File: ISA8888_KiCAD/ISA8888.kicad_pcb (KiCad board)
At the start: 2 copper layers, 154.8 x 106.2 mm, 65 parts, among them J1 Bus_PCI_32bit_Universal, J2 Bus_ISA_16bit, J3 AEN/BALE/TC J3, J4 Crystal J4, J5 PCI Jumpers, J6 PPDGNT# Motherboard Redirect, J7 PPDREQ# Motherboard Redirect, U2 SMROM-AT24CS02, U3 -5v MAX660, Y1 CFPS-72

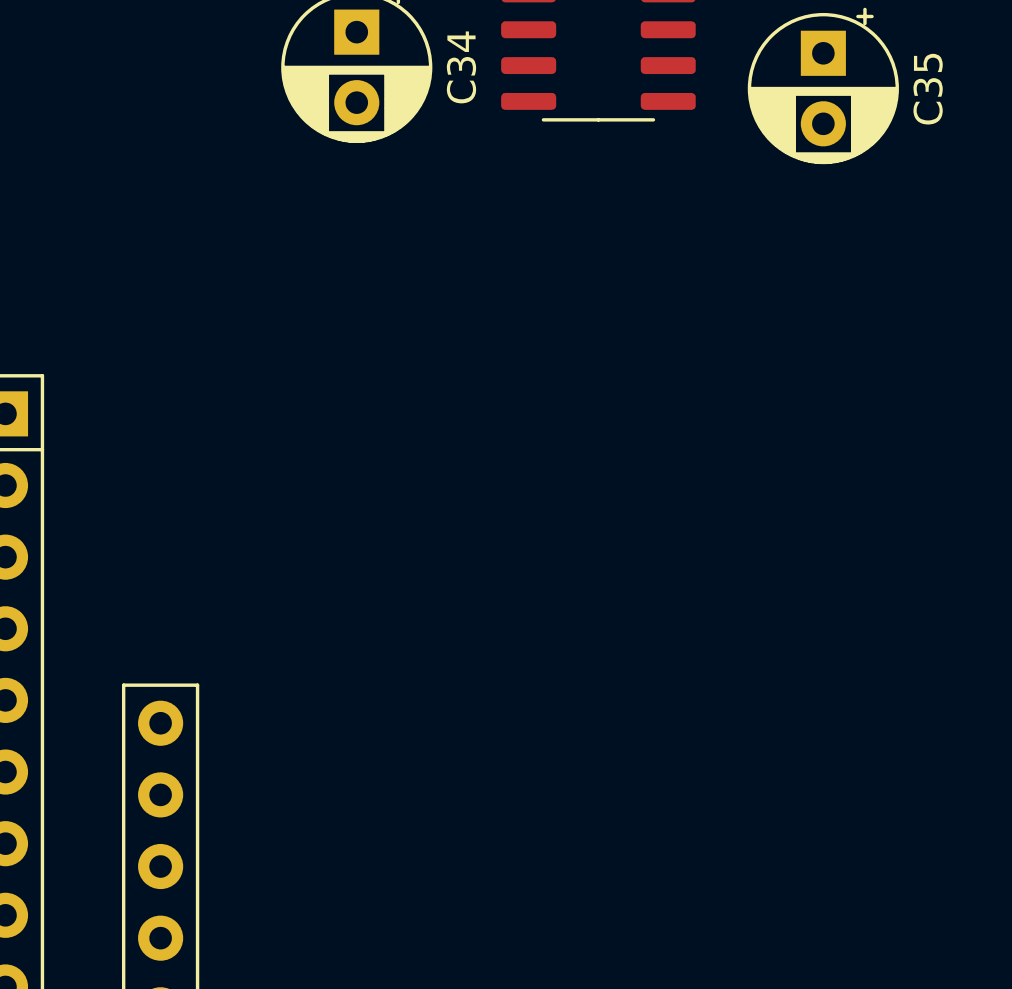
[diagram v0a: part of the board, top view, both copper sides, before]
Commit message: New SCH sheet "Power and Configuration"
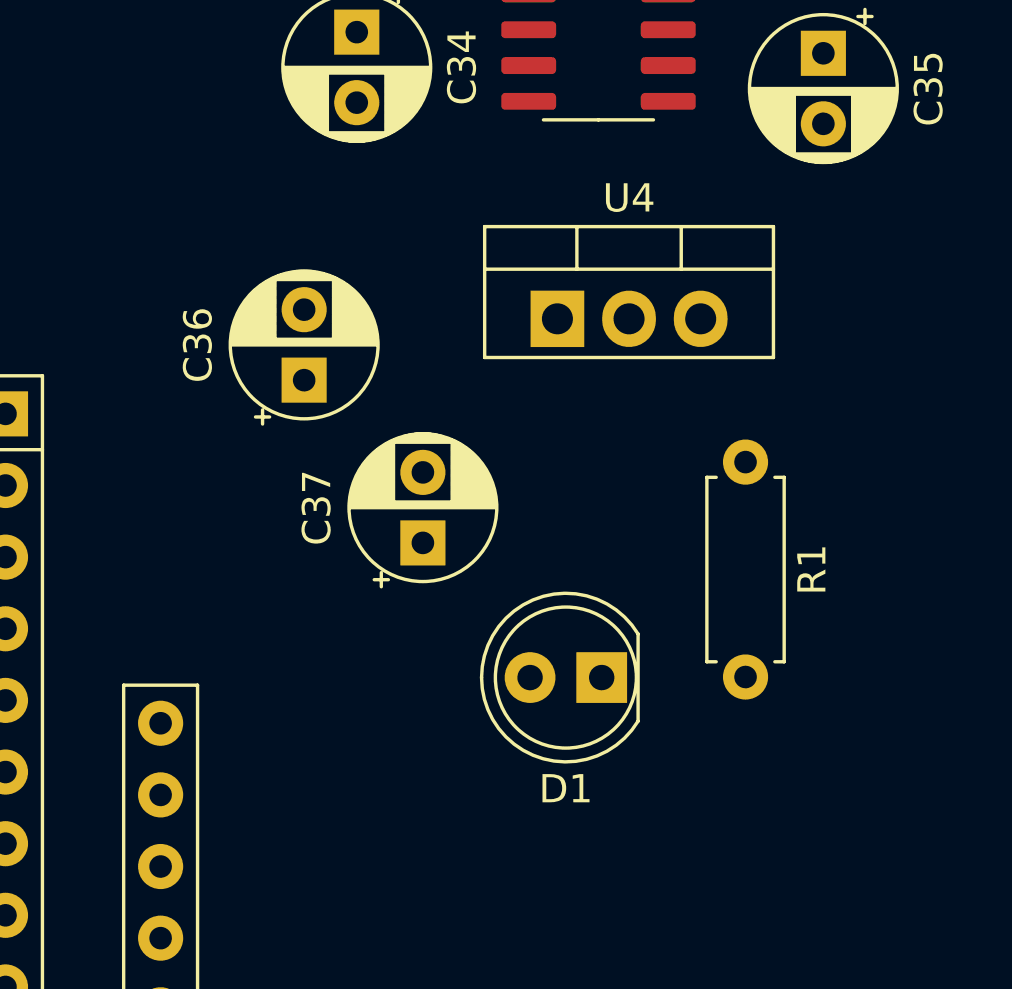
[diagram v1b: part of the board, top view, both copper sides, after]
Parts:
- added C36: 33uF, Capacitor_THT:CP_Radial_D5.0mm_P2.50mm, F.Cu at (209.8, 88.4)
- added C37: 33uF, Capacitor_THT:CP_Radial_D5.0mm_P2.50mm, F.Cu at (214.1, 94.2)
- added D1: -5V, LED_THT:LED_D5.0mm, F.Cu at (220.4, 98.9)
- added R1: 330, Resistor_THT:R_Axial_DIN0207_L6.3mm_D2.5mm_P7.62mm_Horizontal, F.Cu at (225.5, 91.3)
- added U4: LM7905_TO220, Package_TO_SOT_THT:TO-220-3_Vertical, F.Cu at (218.8, 86.2)
- U3: value -5v MAX660 -> ~
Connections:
- J2 pad 4: unconnected-(J2-IRQ2-Pad4) -> IRQ9

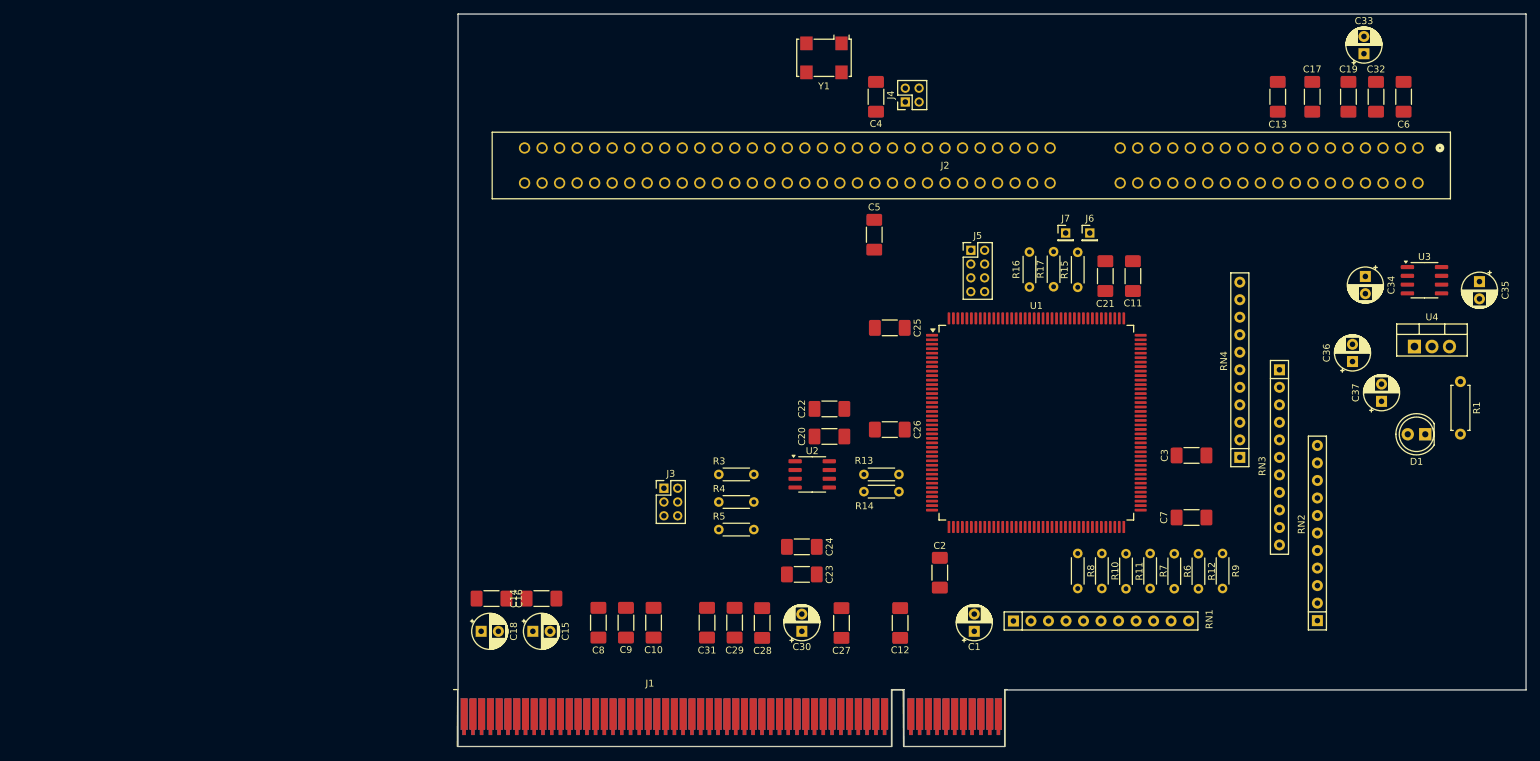
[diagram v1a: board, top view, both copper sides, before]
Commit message: Fixup Power/Config Sheet and update PCB with info from P/C sheet
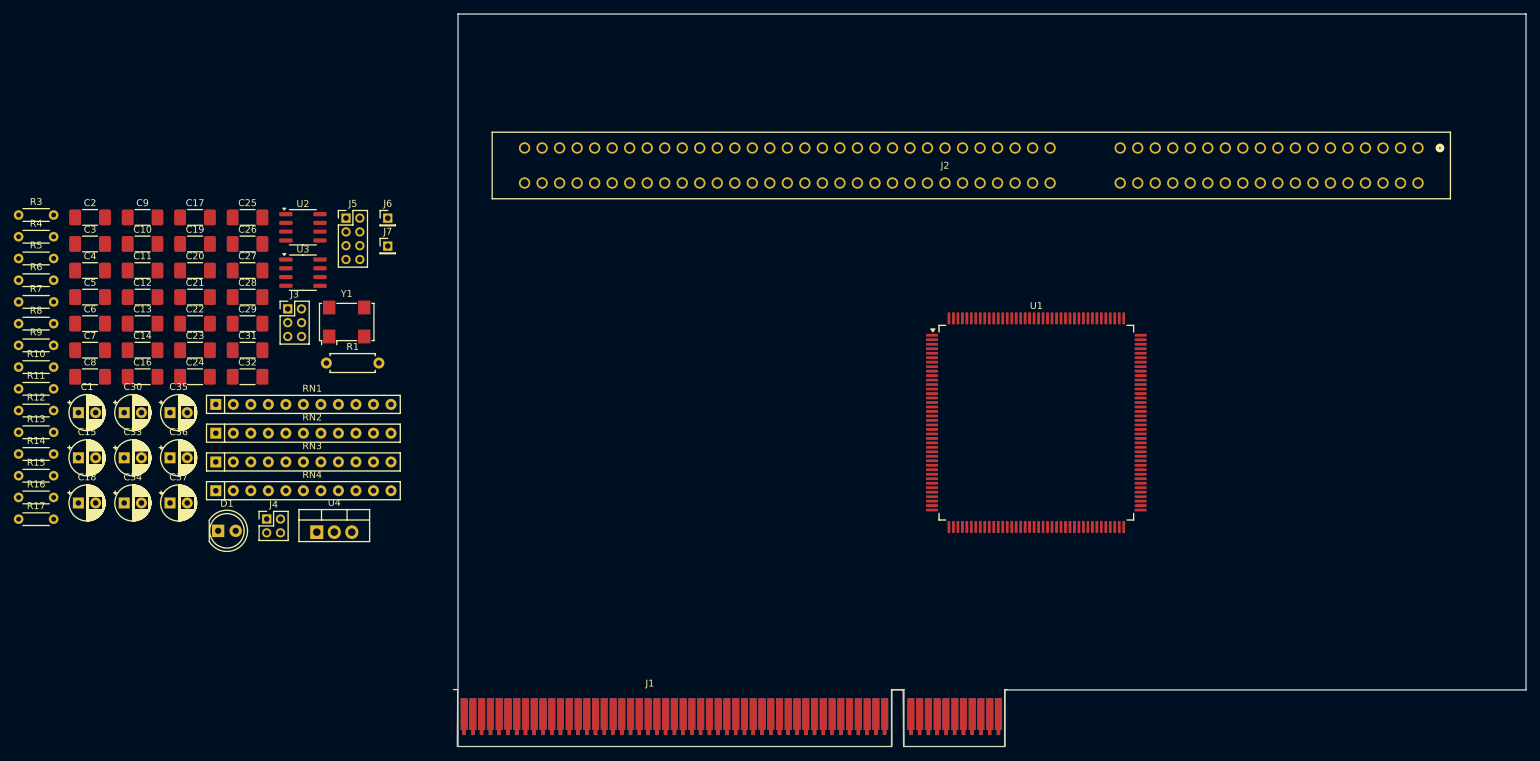
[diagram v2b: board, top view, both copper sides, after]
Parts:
- moved C6 193.3 mm to (26.8, 82.9), turned to 0 degrees
- moved C35 190.8 mm to (38.4, 95.8), turned to 0 degrees
- moved C33 189.1 mm to (31.7, 102.3), turned to 0 degrees
- moved C34 182.9 mm to (31.7, 108.9), turned to 0 degrees
- moved R9 177.1 mm to (16.4, 86.0), turned to 0 degrees
- moved C37 176.3 mm to (38.4, 108.9), turned to 0 degrees
- moved D1 175.6 mm to (45.4, 112.9), turned to 0 degrees
- moved R12 172.3 mm to (16.4, 95.5), turned to 0 degrees
- moved R6 172.2 mm to (16.4, 76.6), turned to 0 degrees
- moved C36 172.0 mm to (38.4, 102.3), turned to 0 degrees
- moved C19 168.6 mm to (42.0, 71.3), turned to 0 degrees
- moved C32 168.6 mm to (49.6, 90.6), turned to 0 degrees
- moved R7 168.1 mm to (16.4, 79.7), turned to 0 degrees
- moved C13 167.8 mm to (34.4, 82.9), turned to 0 degrees
- moved R1 164.5 mm to (61.1, 88.6), turned to 0 degrees
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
